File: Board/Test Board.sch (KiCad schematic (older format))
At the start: 19 parts, among them J1 SCREW TERMINAL, J2 SCREW TERMINAL, J3 SCREW TERMINAL, U1 LM2596T-5, U2 L293D, U3 DS1E-M-DC5V, U4 DS1E-M-DC5V, U5 DS1E-M-DC5V, U6 DHT11

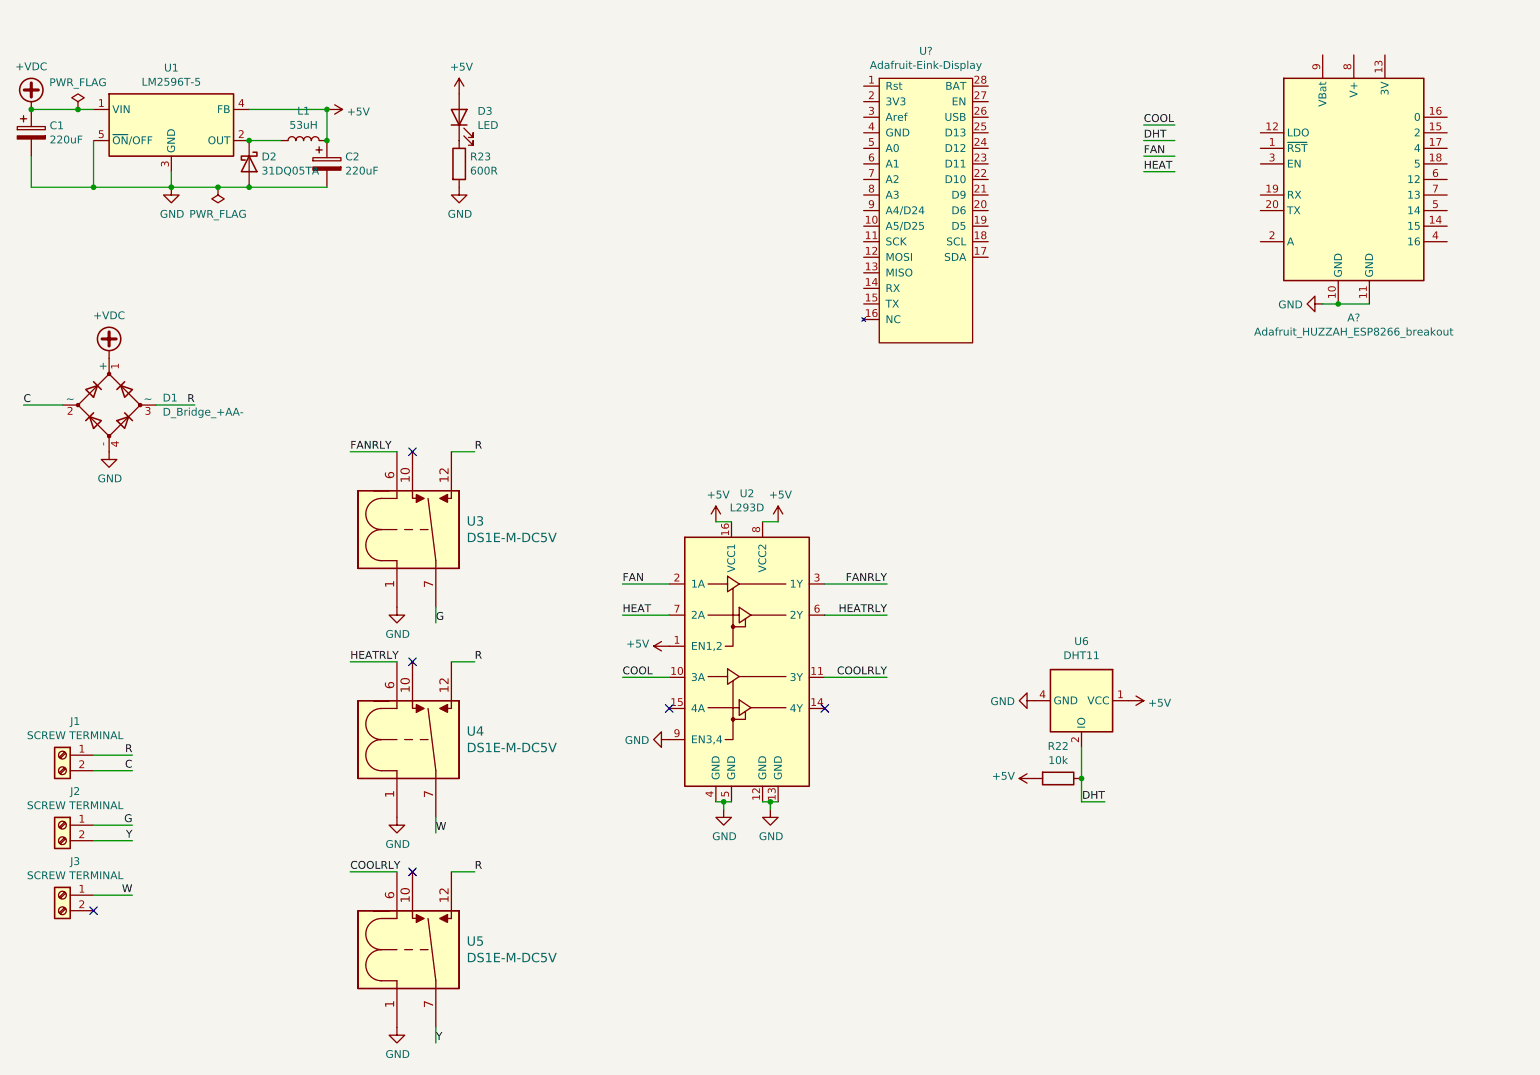
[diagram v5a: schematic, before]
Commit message: Continued E-Ink display transition
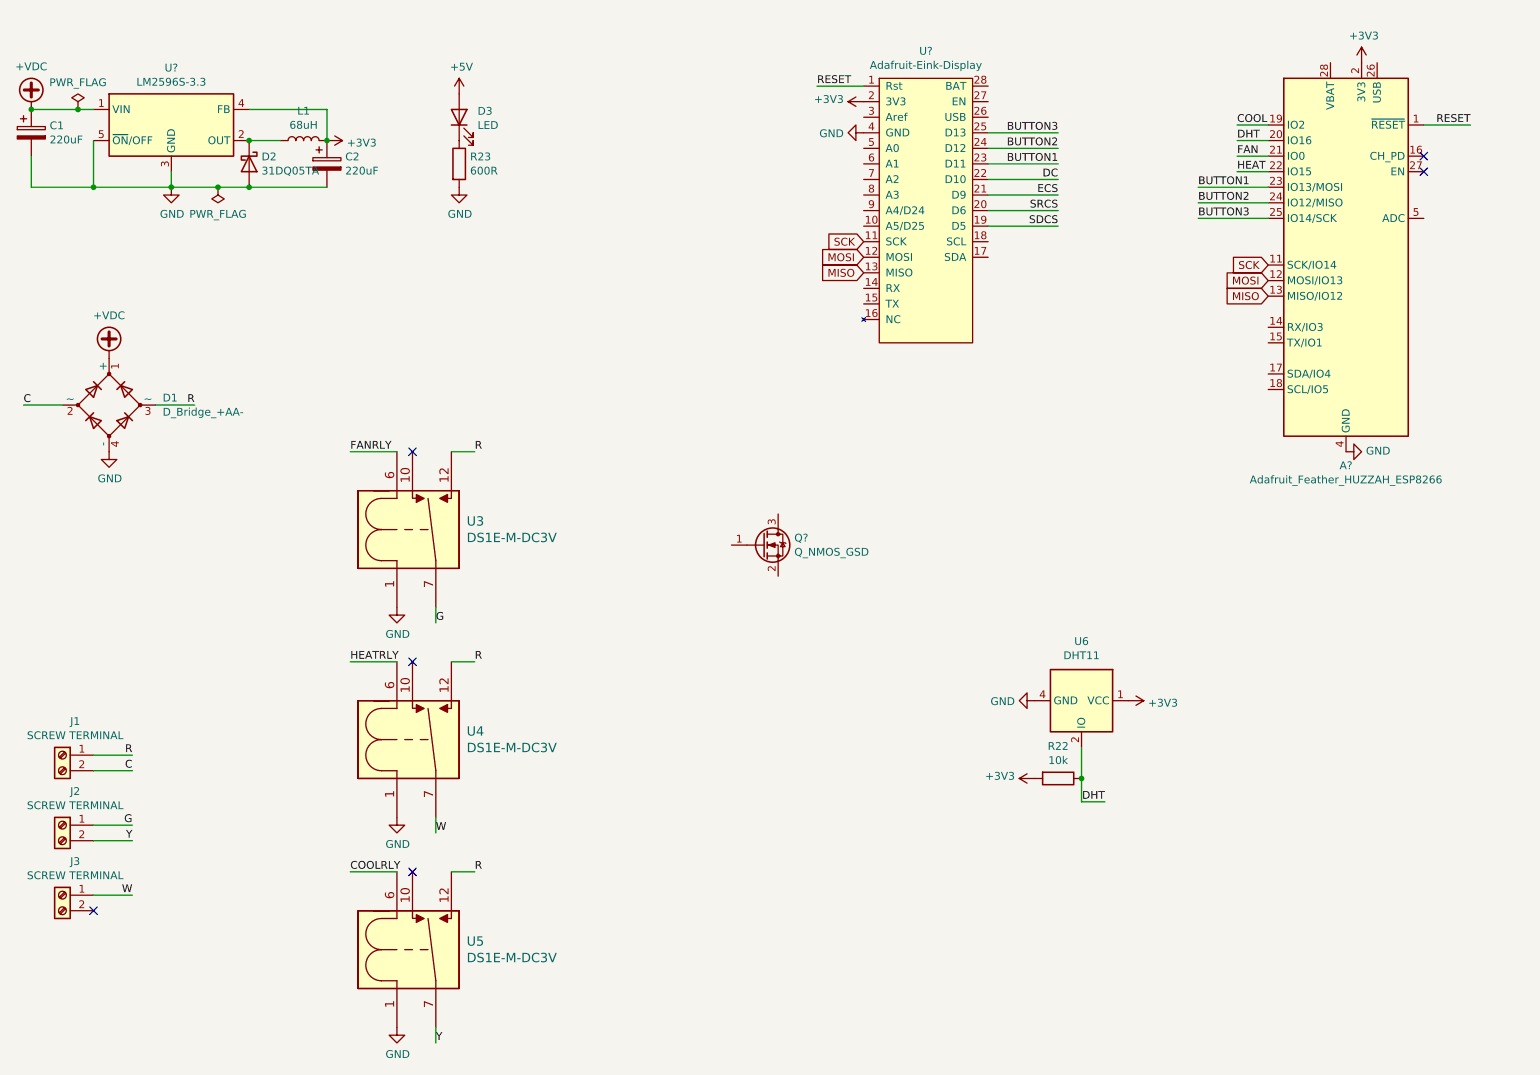
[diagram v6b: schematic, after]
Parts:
- removed A?: Adafruit_HUZZAH_ESP8266_breakout, symbol MCU_Module:Adafruit_HUZZAH_ESP8266_breakout
- removed U1: LM2596T-5, Package_TO_SOT_THT:TO-220-5_P3.4x3.7mm_StaggerOdd_Lead3.8mm_Vertical, symbol Regulator_Switching:LM2596T-5
- removed U2: L293D, Package_DIP:DIP-16_W7.62mm, symbol Driver_Motor:L293D
- added A?: Adafruit_Feather_HUZZAH_ESP8266, Module:Adafruit_Feather, symbol MCU_Module:Adafruit_Feather_HUZZAH_ESP8266
- added Q?: Q_NMOS_GSD, symbol Device:Q_NMOS_GSD
- added U?: LM2596S-3.3, Package_TO_SOT_SMD:TO-263-5_TabPin3, symbol Regulator_Switching:LM2596S-3.3
- L1: value 53uH -> 68uH
- U3, U4, U5: value DS1E-M-DC5V -> DS1E-M-DC3V
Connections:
- net labels added: +3V3, BUTTON1, BUTTON2, BUTTON3, DC, ECS, MISO, MOSI, RESET, SCK, SDCS, SRCS
- wire segments 52 -> 48

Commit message: Finish Schematic for new PCB
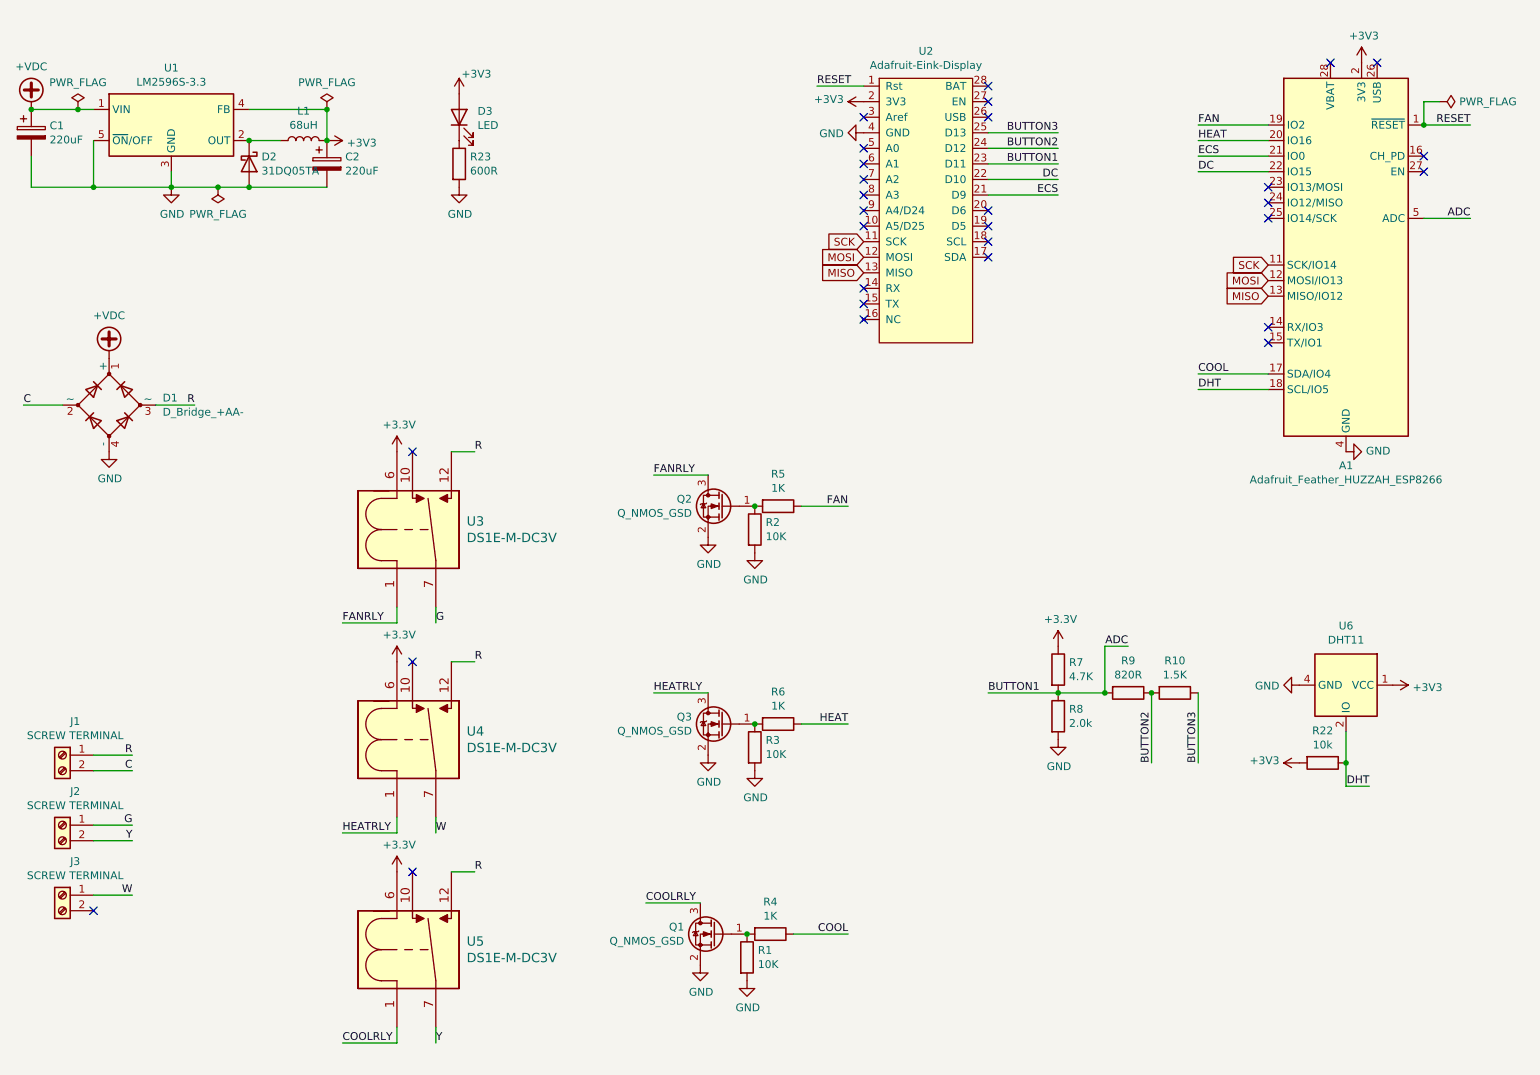
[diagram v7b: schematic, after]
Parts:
- added Q1, Q3: Q_NMOS_GSD, Package_TO_SOT_SMD:SOT-23, symbol Device:Q_NMOS_GSD
- added R1, R2, R3: 10K, Resistor_SMD:R_1206_3216Metric, symbol Device:R
- added R10: 1.5K, Resistor_SMD:R_1206_3216Metric, symbol Device:R
- added R4, R5, R6: 1K, Resistor_SMD:R_1206_3216Metric, symbol Device:R
- added R7: 4.7K, Resistor_SMD:R_1206_3216Metric, symbol Device:R
- added R8: 2.0k, Resistor_SMD:R_1206_3216Metric, symbol Device:R
- added R9: 820R, Resistor_SMD:R_1206_3216Metric, symbol Device:R
- L1: footprint Inductor_THT:L_Radial_D12.0mm_P5.00mm_Fastron_11P -> Inductor_THT:L_Toroid_Horizontal_D24.1mm_P21.80mm_Bourns_2200
- Q2: renamed from Q?; footprint (none) -> Package_TO_SOT_SMD:SOT-23
- U2: renamed from U?; footprint (none) -> Arduino-Thermostat:Adafruit-eink-display
- gave numbers to parts that had none: 2
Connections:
- net +5V is gone; now on net +3V3: D3.2 (A)
- net +3V3: now also U3.6, U4.6, U5.6, R7.1
- net BUTTON2: now also R10.2, R9.1; no longer A1.24 (IO12/MISO)
- net BUTTON3: now also R10.1; no longer A1.25 (IO14/SCK)
- net COOL: now also A1.17 (SDA/IO4), R4.1; no longer A1.19 (IO2)
- net COOLRLY: now also U5.1, Q1.3 (D); no longer U5.6
- net DC: now also A1.22 (IO15)
- net DHT: now also A1.18 (SCL/IO5); no longer A1.20 (IO16)
- net ECS: now also A1.21 (IO0)
- net FAN: now also A1.19 (IO2), R5.1; no longer A1.21 (IO0)
- net FANRLY: now also Q2.3 (D), U3.1; no longer U3.6
- net GND: now also Q2.2 (S), Q1.2 (S), Q3.2 (S), R1.2, R2.2, R3.2, R8.2; no longer U3.1, U4.1, U5.1
- net HEAT: now also A1.20 (IO16), R6.1; no longer A1.22 (IO15)
- net HEATRLY: now also U4.1, Q3.3 (D); no longer U4.6
- net ADC: now reaches A1.5 (ADC)
- net ADC: now also U2.23 (D11), R7.2, R8.1, R9.2
- net at Q2.1 (G): now also R2.1, R5.2
- net BUTTON1: no longer names the net of A1.23 (IO13/MOSI)
- net BUTTON1: no longer U2.23 (D11)
- net SDCS: no longer names the net of U2.19 (D5)
- net SRCS: no longer names the net of U2.20 (D6)
- new net: Q3.1 (G), R3.1, R6.2
- new net: Q1.1 (G), R1.1, R4.2
- no-connect marks 6 -> 30
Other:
- moved on the sheet: Q2, R22, U6
